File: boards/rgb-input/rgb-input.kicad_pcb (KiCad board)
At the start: 2 copper layers, 138.9 x 89.2 mm, 174 parts, among them J1 Barrel_Jack, J13 I2C, J42 INPUTS, J46 RGB, U1 ESP32-DEVKITC, U13 MCP1502, U2 MCP3208, U3 XL1509-5.0, U5 TLC5947DAP, U6 TLC5947DAP

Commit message: various cleanups and tidying
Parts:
- moved H3 1.29 mm to (78.0, 53.0)
- moved H4 1.20 mm to (211.0, 53.0)
- moved ADC0 0.50 mm to (128.9, 133.9)
- moved ADC1 0.50 mm to (139.0, 133.9)
- moved ADC2 0.50 mm to (149.2, 133.9)
- moved ADC3 0.50 mm to (159.4, 133.9)
- moved ADC4 0.50 mm to (169.5, 133.9)
- moved ADC5 0.50 mm to (179.7, 133.9)
- moved ADC6 0.50 mm to (189.8, 133.9)
- moved ADC7 0.50 mm to (200.0, 133.9)
- moved C1 0.50 mm to (100.4, 132.6)
- moved C10 0.50 mm to (135.1, 92.5)
- moved C11 0.50 mm to (142.8, 92.5)
- moved C12 0.50 mm to (127.7, 129.3)
- moved C13 0.50 mm to (137.9, 129.3)
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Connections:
- H1 pad 1: (no net) -> unconnected-(H1-Pad1)
- H2 pad 1: (no net) -> unconnected-(H2-Pad1)
- H3 pad 1: (no net) -> unconnected-(H3-Pad1)
- H4 pad 1: (no net) -> unconnected-(H4-Pad1)
- J1 pad MP: (no net) -> GNDD
- J13 pad MP: (no net) -> unconnected-(J13-MountPin-PadMP)
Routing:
- net /LEDS/GREEN4: track 68.4 -> 66.5 mm
- net /LEDS/BLUE4: track 79.1 -> 77.2 mm
- net /LEDS/RED4: track 70.6 -> 68.7 mm
- net /LEDS/RED5: track 69.6 -> 68.0 mm
- net /LEDS/GREEN5: track 65.9 -> 64.4 mm
- net /LEDS/BLUE5: track 65.6 -> 64.2 mm
- net /LEDS/BLUE3: track 50.1 -> 50.7 mm
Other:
- board size 138.9 x 89.2 mm -> 139 x 90 mm

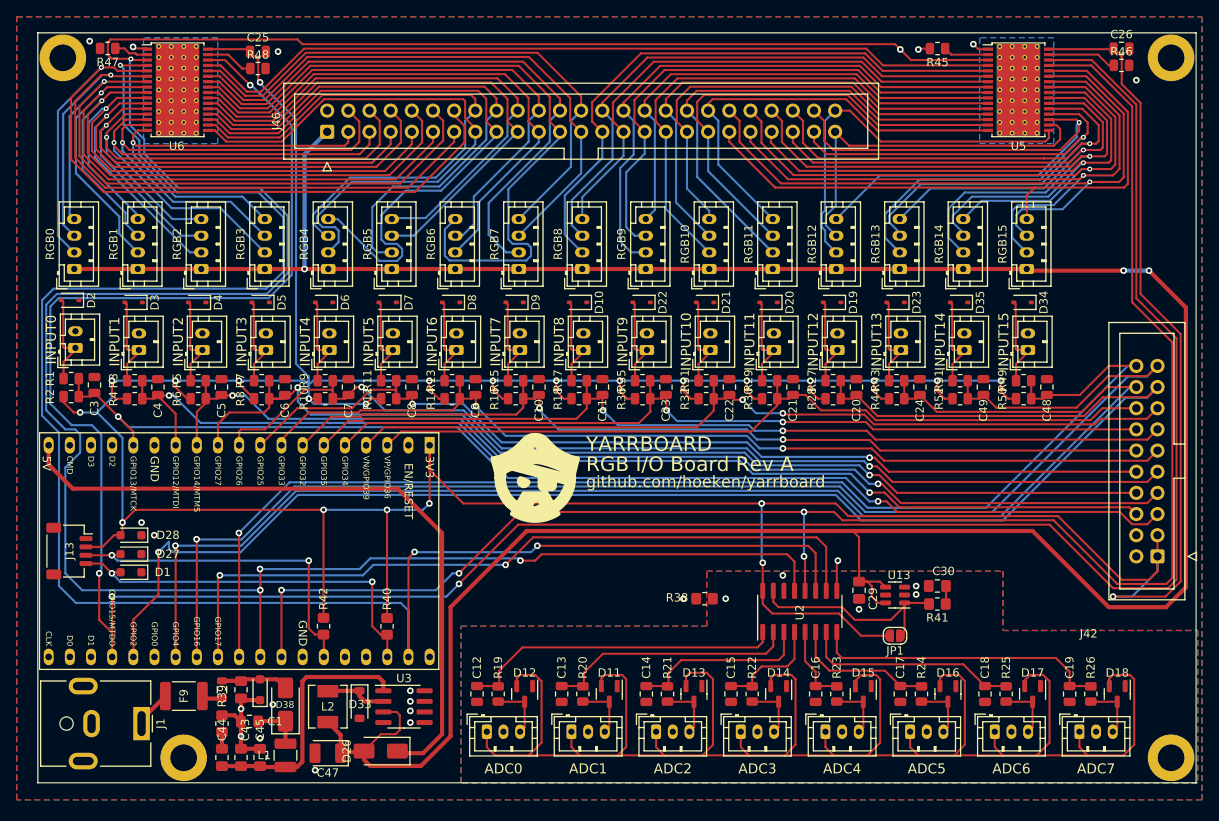
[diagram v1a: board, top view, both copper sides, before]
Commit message: added 5v fuse to schematic
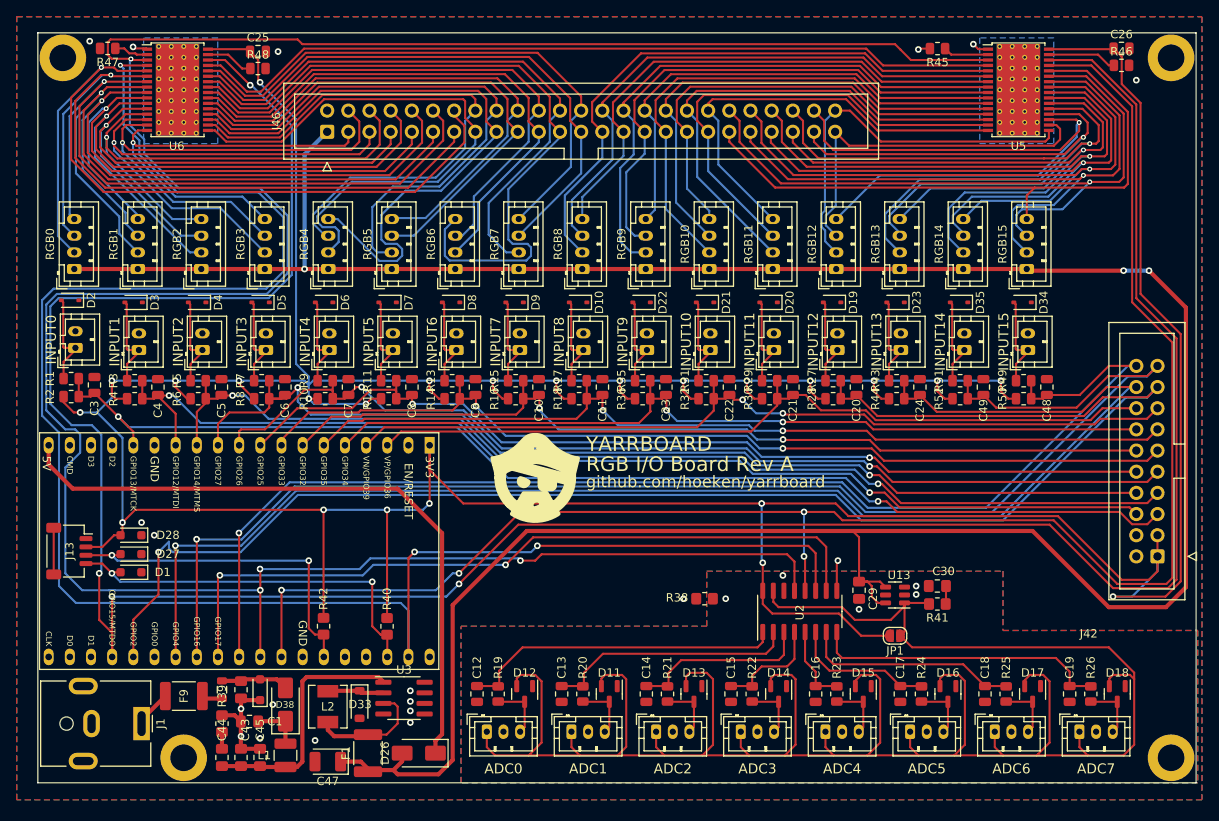
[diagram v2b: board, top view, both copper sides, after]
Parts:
- added F1: mSMD100, Fuse:Fuse_1812_4532Metric_Pad1.30x3.40mm_HandSolder, F.Cu at (114.6, 136.4)
- F9: value MD050-60V -> mSMD050-60V
- moved D26 4.58 mm to (120.7, 136.4)
- moved U3 1.02 mm to (118.9, 129.8)
- moved C47 1.01 mm to (109.8, 137.5)
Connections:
- ADC0 pad 1: +3V3 -> REF_3V3
- ADC1 pad 1: +3V3 -> REF_3V3
- ADC2 pad 1: +3V3 -> REF_3V3
- ADC3 pad 1: +3V3 -> REF_3V3
- ADC4 pad 1: +3V3 -> REF_3V3
- ADC5 pad 1: +3V3 -> REF_3V3
- ADC6 pad 1: +3V3 -> REF_3V3
- ADC7 pad 1: +3V3 -> REF_3V3
- D11 pad 2: +3V3 -> REF_3V3
- D12 pad 2: +3V3 -> REF_3V3
- D13 pad 2: +3V3 -> REF_3V3
- D14 pad 2: +3V3 -> REF_3V3
- D15 pad 2: +3V3 -> REF_3V3
- D16 pad 2: +3V3 -> REF_3V3
- D17 pad 2: +3V3 -> REF_3V3
- D18 pad 2: +3V3 -> REF_3V3
- L2 pad 2: +5V -> Net-(U3-FB)
- U3 pad 3: +5V -> Net-(U3-FB)
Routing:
- net REF_3V3: track 26.2 -> 269.8 mm
- net +3V3: track 213.0 -> 0.00 mm
- net Net-(U3-FB): track 0.00 -> 14.2 mm
- net +5V: track 343.3 -> 333.9 mm
- net unconnected-(J13-MountPin-PadMP): track 0.00 -> 5.60 mm
- net ESP32_VIN: track 83.5 -> 79.7 mm
- net Net-(U3-VIN): track 30.9 -> 29.8 mm
- net Net-(D33-K): track 7.59 -> 6.79 mm
- net SCK: vias 5 -> 4

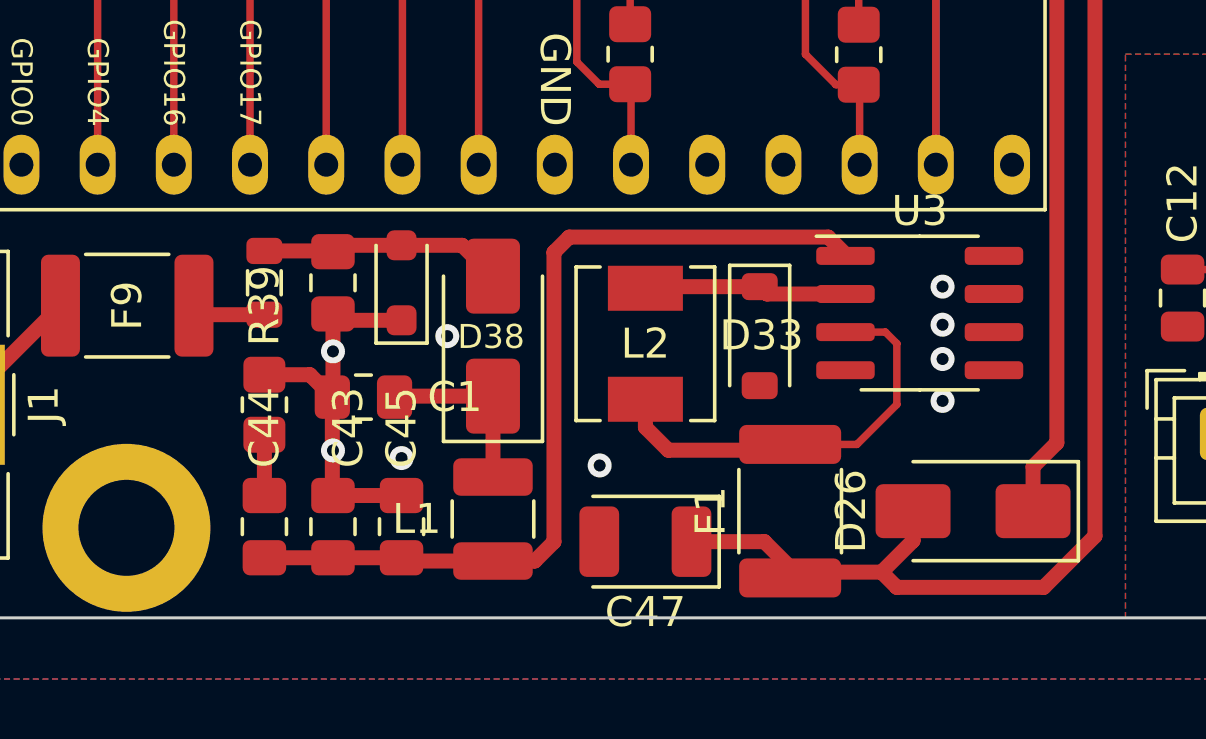
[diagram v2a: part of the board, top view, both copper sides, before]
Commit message: updated layout with new fuse.
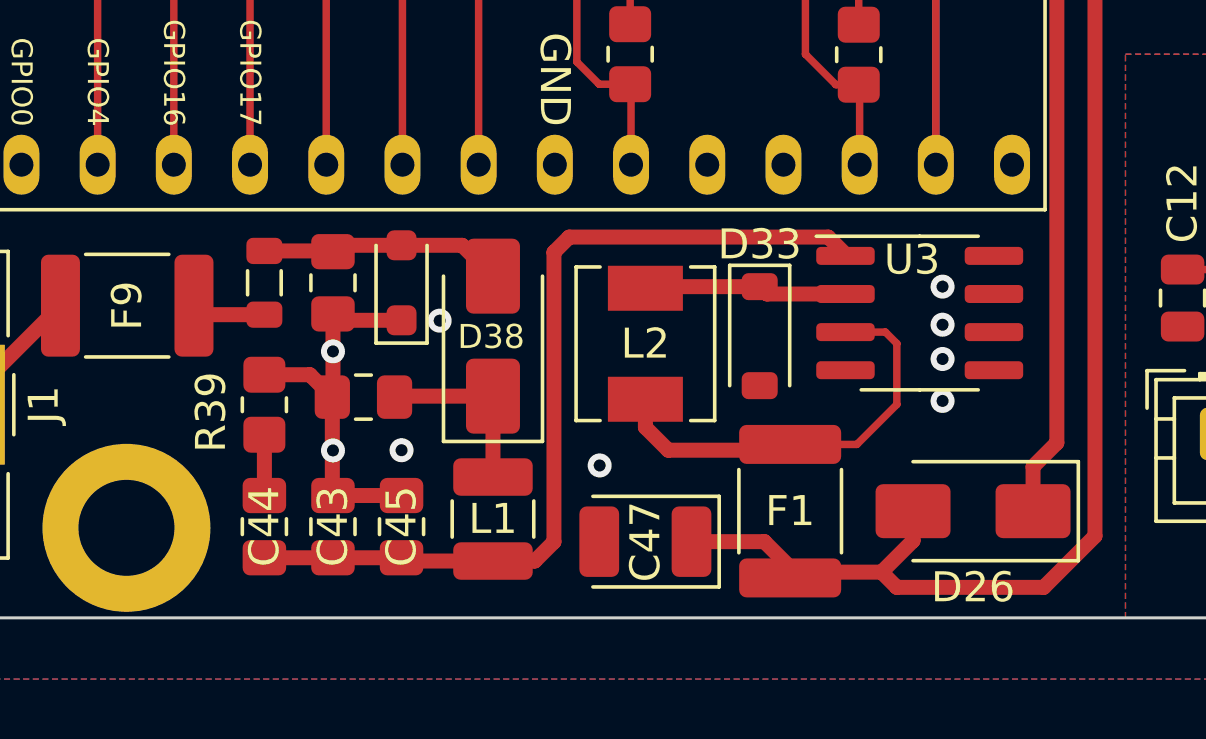
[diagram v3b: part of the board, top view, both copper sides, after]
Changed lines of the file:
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@@
     (property "ki_keywords" "capacitor cap")
     (attr smd)
-    (fp_text reference "C45" (at 3.302 0 90) (layer "F.SilkS")
+    (fp_text reference "C45" (at 0.008 0 90) (layer "F.SilkS")
         (effects (font (size 1 1) (thickness 0.15)))
     )
@@
     (property "ki_keywords" "capacitor cap")
     (attr smd)
-    (fp_text reference "C44" (at 3.302 0 90) (layer "F.SilkS")
+    (fp_text reference "C44" (at 0.008 0 90) (layer "F.SilkS")
         (effects (font (size 1 1) (thickness 0.15)))
     )
@@
     (property "ki_keywords" "resettable fuse PTC PPTC polyfuse polyswitch")
     (attr smd)
-    (fp_text reference "F1" (at 0 -2.65 90) (layer "F.SilkS")
+    (fp_text reference "F1" (at 0 0) (layer "F.SilkS")
         (effects (font (size 1 1) (thickness 0.15)))
     )
@@
     (property "ki_keywords" "capacitor cap")
     (attr smd)
-    (fp_text reference "C2" (at 3.048 0 90) (layer "Dwgs.User")
+    (fp_text reference "C2" (at -0.008 0 90) (layer "Dwgs.User")
         (effects (font (size 1 1) (thickness 0.15)))
     )
@@
     (property "ki_keywords" "inductor choke coil reactor magnetic")
     (attr smd)
-    (fp_text reference "L1" (at 0 2.54) (layer "F.SilkS")
+    (fp_text reference "L1" (at 0 0) (layer "F.SilkS")
         (effects (font (size 1 1) (thickness 0.15)))
     )
@@
     (property "ki_keywords" "diode Schottky")
     (attr smd)
-    (fp_text reference "D33" (at -0.023 -0.062) (layer "F.SilkS")
+    (fp_text reference "D33" (at -3.056 0) (layer "F.SilkS")
         (effects (font (size 1 1) (thickness 0.15)))
     )
@@
     (property "ki_keywords" "Buck DC/DC Converter")
     (attr smd)
-    (fp_text reference "U3" (at 0 -3.4) (layer "F.SilkS")
+    (fp_text reference "U3" (at -0.254 -1.778) (layer "F.SilkS")
         (effects (font (size 1 1) (thickness 0.15)))
     )
@@
     (property "ki_keywords" "L ferrite bead inductor filter")
     (attr smd)
-    (fp_text reference "FB7" (at -3.302 0.023 90) (layer "Dwgs.User")
+    (fp_text reference "FB7" (at -0.246 0 90) (layer "Dwgs.User")
         (effects (font (size 1 1) (thickness 0.15)))
     )
@@
     (property "ki_keywords" "r resistor")
     (attr smd)
-    (fp_text reference "R39" (at 3.302 0 90) (layer "F.SilkS")
+    (fp_text reference "R39" (at -0.246 -1.778 90) (layer "F.SilkS")
         (effects (font (size 1 1) (thickness 0.15)))
     )
@@
     (property "ki_keywords" "capacitor cap")
     (attr smd)
-    (fp_text reference "C1" (at -3.048 0) (layer "F.SilkS")
+    (fp_text reference "C1" (at 0 0.008) (layer "Dwgs.User")
         (effects (font (size 1 1) (thickness 0.15)))
     )
@@
     (property "ki_keywords" "cap capacitor")
     (attr smd)
-    (fp_text reference "C47" (at 0 -2.35) (layer "F.SilkS")
+    (fp_text reference "C47" (at 0 0 90) (layer "F.SilkS")
         (effects (font (size 1 1) (thickness 0.15)))
     )
@@
     (property "ki_keywords" "diode TVS thyrector")
     (attr smd)
-    (fp_text reference "D32" (at -0.062 -2.136 90) (layer "Dwgs.User")
+    (fp_text reference "D32" (at -0.062 0 90) (layer "Dwgs.User")
         (effects (font (size 1 1) (thickness 0.15)))
     )
@@
     (property "ki_keywords" "diode Schottky")
     (attr smd)
-    (fp_text reference "D26" (at 4.064 0 90) (layer "F.SilkS")
+    (fp_text reference "D26" (at 0 -2.54 180) (layer "F.SilkS")
         (effects (font (size 1 1) (thickness 0.15)))
     )
@@
     (property "ki_keywords" "capacitor cap")
     (attr smd)
-    (fp_text reference "C43" (at 3.302 0.508 90) (layer "F.SilkS")
+    (fp_text reference "C43" (at 0.008 0 90) (layer "F.SilkS")
         (effects (font (size 1 1) (thickness 0.15)))
     )
@@
   )
   (dimension (type aligned) (layer "Dwgs.User")
+    (pts (xy 88.716 140) (xy 125.038 140))
+    (height 3.556)
+    (gr_text "36.3220 mm" (at 106.877 142.406) (layer "Dwgs.User")
+      (effects (font (size 1 1) (thickness 0.15)))
+    )
+    (format (prefix "") (suffix "") (units 3) (units_format 1) (precision 4))
+    (style (thickness 0.15) (arrow_length 1.27) (text_position_mode 0) (extension_height 0.58642) (extension_offset 0.5) keep_text_aligned)
+  )
+  (dimension (type aligned) (layer "Dwgs.User")
     (pts (xy 75 140) (xy 214 140))
     (height 5.079999)
@@
   )
   (dimension (type aligned) (layer "Dwgs.User")
+    (pts (xy 88.946 126.896) (xy 88.946 138.896))
+    (height 3.532)
+    (gr_text "12.0000 mm" (at 84.264 132.896 90) (layer "Dwgs.User")
+      (effects (font (size 1 1) (thickness 0.15)))
+    )
+    (format (prefix "") (suffix "") (units 3) (units_format 1) (precision 4))
+    (style (thickness 0.15) (arrow_length 1.27) (text_position_mode 0) (extension_height 0.58642) (extension_offset 0.5) keep_text_aligned)
+  )
+  (dimension (type aligned) (layer "Dwgs.User")
     (pts (xy 75 140) (xy 75 50))
     (height -3.302)
@@
   (via (at 86.43 51.689) (size 0.8) (drill 0.4) (layers "F.Cu" "B.Cu") (free) (net 3))
   (via (at 187.268 51.362) (size 0.8) (drill 0.4) (layers "F.Cu" "B.Cu") (free) (net 3))
-  (via (at 101.67 134.674) (size 0.8) (drill 0.4) (layers "F.Cu" "B.Cu") (free) (net 3))
+  (via (at 101.67 134.412) (size 0.8) (drill 0.4) (layers "F.Cu" "B.Cu") (free) (net 3))
   (via (at 119.704 132.769) (size 0.8) (drill 0.4) (layers "F.Cu" "B.Cu") (free) (net 3))
   (via (at 81.223 51) (size 0.8) (drill 0.4) (layers "F.Cu" "B.Cu") (free) (net 3))
@@
   (via (at 103.829 52.251) (size 0.8) (drill 0.4) (layers "F.Cu" "B.Cu") (free) (net 3))
   (via (at 152.47 117.91) (size 0.8) (drill 0.4) (layers "F.Cu" "B.Cu") (free) (net 3))
-  (via (at 103.194 130.61) (size 0.8) (drill 0.4) (layers "F.Cu" "B.Cu") (free) (net 3))
+  (via (at 102.94 130.094) (size 0.8) (drill 0.4) (layers "F.Cu" "B.Cu") (free) (net 3))
   (via (at 119.704 130.229) (size 0.8) (drill 0.4) (layers "F.Cu" "B.Cu") (free) (net 3))
   (via (at 99.384 131.118) (size 0.8) (drill 0.4) (layers "F.Cu" "B.Cu") (net 3))

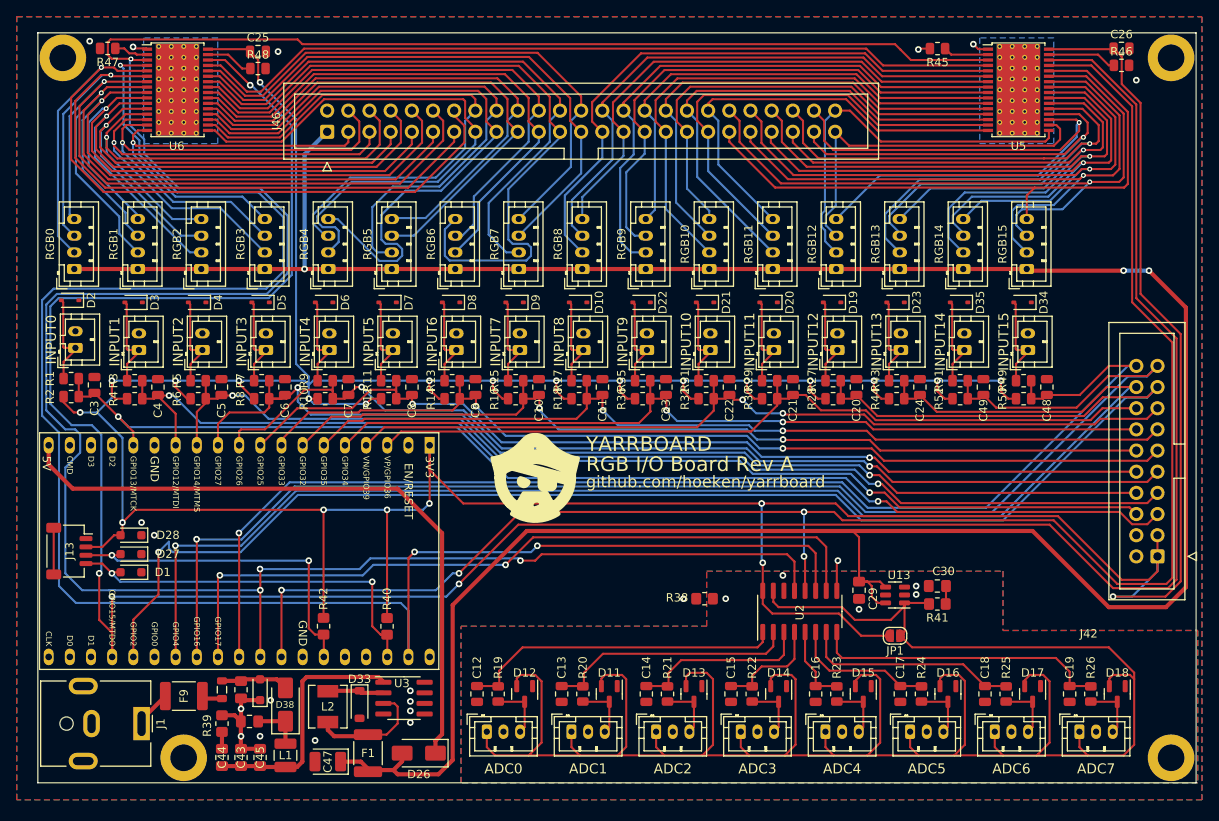
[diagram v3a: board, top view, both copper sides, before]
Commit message: rgb input board ready for production too.
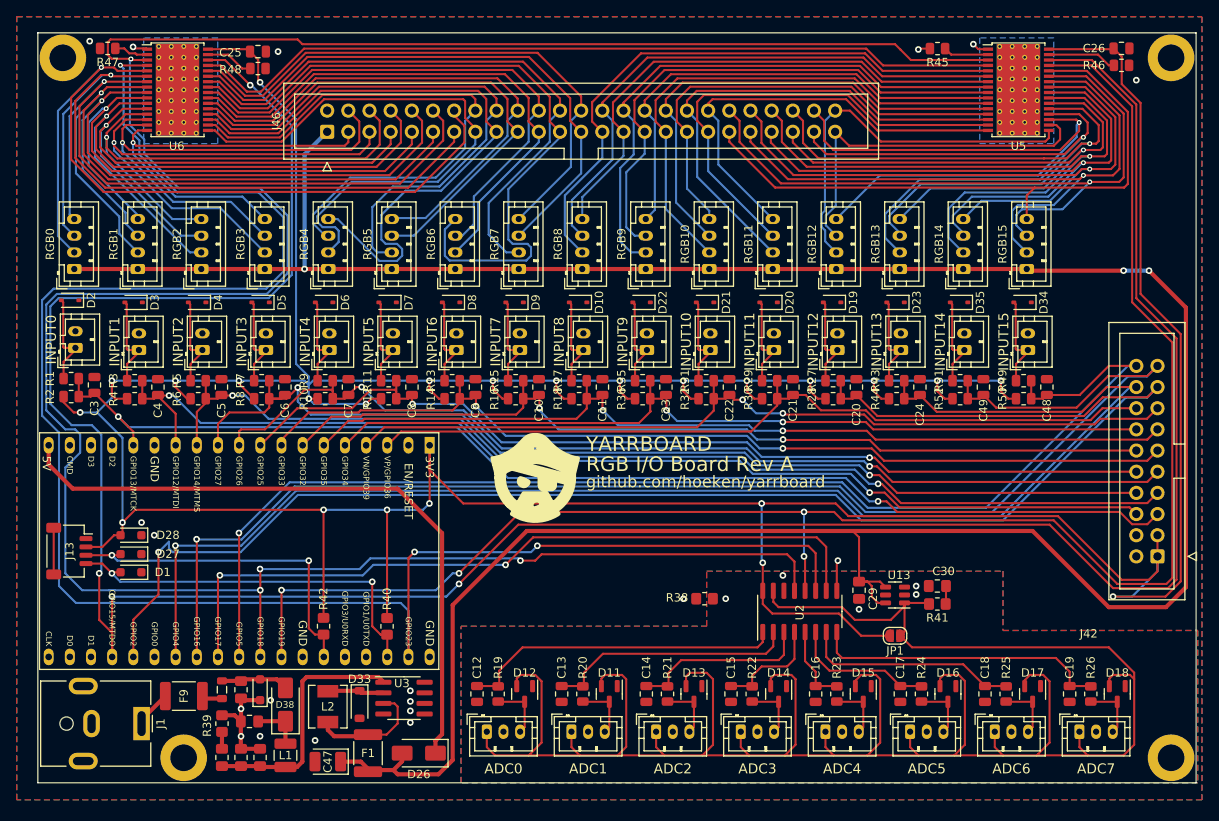
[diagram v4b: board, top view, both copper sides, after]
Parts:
- LOGO: footprint gnarboard:Logo Small -> yarrboard:Logo Small
- U1: footprint gnarboard:ESP32-DevKitC -> yarrboard:ESP32-DevKitC
